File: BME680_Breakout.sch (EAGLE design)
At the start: 19 parts, among them U1 BME680, U4 PCA9515ADP, U8 LD1117XX

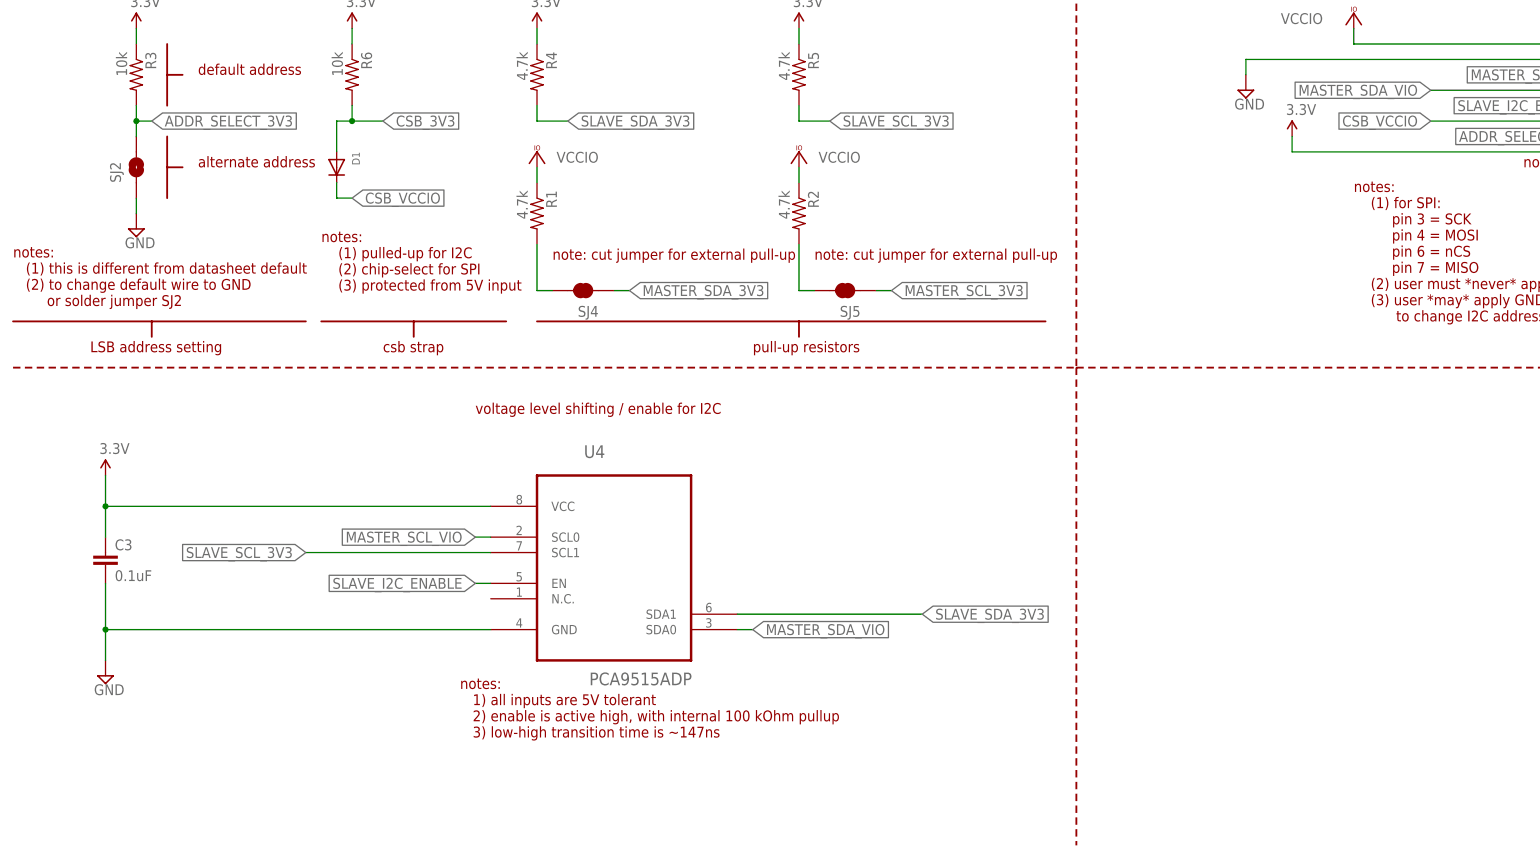
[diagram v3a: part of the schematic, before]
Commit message: added pull-down hardware option to allow changing default behavior of i2c buffer
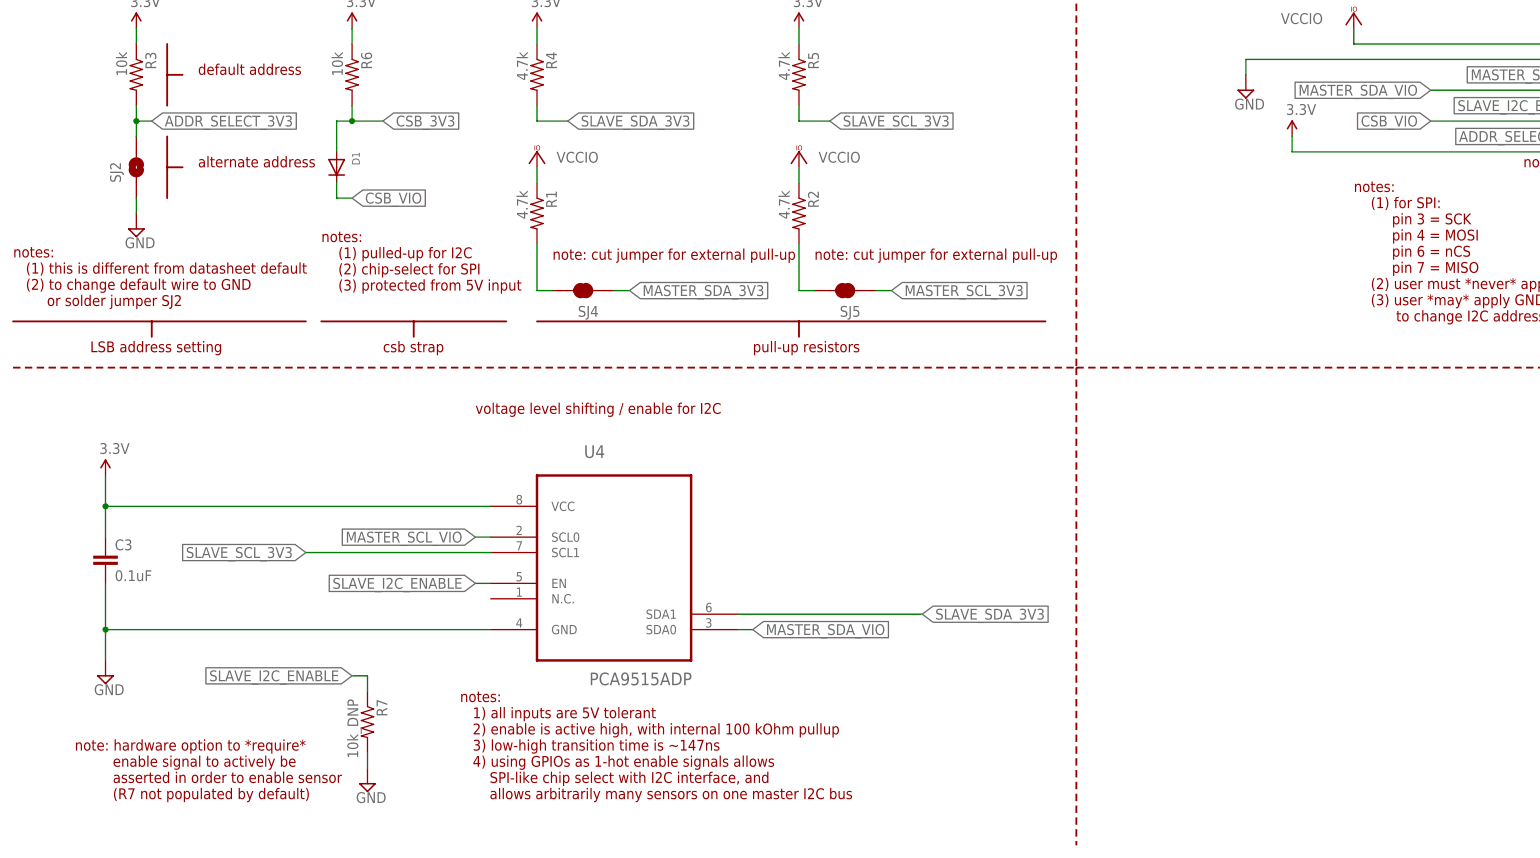
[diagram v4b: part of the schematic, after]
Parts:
- added R7: 10k_DNP, SparkFun-Passives:RESISTOR0805-RES
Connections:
- net CSB_VCCIO renamed CSB_VIO
- net GND: now also R7.2
- net SLAVE_I2C_ENABLE: now also R7.1
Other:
- note added: "note: hardware option to *require* enable signal to actively be asserted in order to enable sensor (R7 not populated by default)"
- note added: "notes: 1) all inputs are 5V tolerant 2) enable is active high, with internal 100 kOhm pullup 3) low-high transition time is ~147ns 4) using GPIOs as 1-hot enable signals allows SPI-like chip select with I2C interface, and allows arbitrarily many sensors on one master I2C bus"
- note removed: "notes: 1) all inputs are 5V tolerant 2) enable is active high, with internal 100 kOhm pullup 3) low-high transition time is ~147ns"
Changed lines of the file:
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@@
 <part name="C4" library="SparkFun-Passives" deviceset="CAP" device="0805" value="10uF"/>
 <part name="C5" library="SparkFun-Passives" deviceset="CAP" device="0805" value="10uF"/>
+<part name="R7" library="SparkFun-Passives" deviceset="RESISTOR" device="0805-RES" value="10k_DNP"/>
+<part name="SUPPLY16" library="supply2" deviceset="GND" device=""/>
 </parts>
 <sheets>
@@
     (2) chip-select for SPI
     (3) protected from 5V input</text>
-<text x="116.84" y="53.34" size="1.778" layer="94">notes:
+<text x="116.84" y="43.18" size="1.778" layer="94">notes:
    1) all inputs are 5V tolerant
    2) enable is active high, with internal 100 kOhm pullup
-   3) low-high transition time is ~147ns</text>
+   3) low-high transition time is ~147ns
+   4) using GPIOs as 1-hot enable signals allows
+       SPI-like chip select with I2C interface, and
+       allows arbitrarily many sensors on one master I2C bus</text>
 <text x="292.1" y="147.32" size="1.778" layer="94">note: output!</text>
 <text x="264.16" y="121.92" size="1.778" layer="94">notes:
@@
 <text x="132.08" y="132.08" size="1.778" layer="94">note: cut jumper for external pull-up</text>
 <text x="175.26" y="132.08" size="1.778" layer="94">note: cut jumper for external pull-up</text>
+<text x="53.34" y="43.18" size="1.778" layer="94">note: hardware option to *require*
+         enable signal to actively be
+         asserted in order to enable sensor
+         (R7 not populated by default)</text>
 </plain>
 <instances>
@@
 <instance part="C4" gate="G$1" x="264.16" y="215.9"/>
 <instance part="C5" gate="G$1" x="297.18" y="215.9"/>
+<instance part="R7" gate="G$1" x="101.6" y="55.88" rot="R270"/>
+<instance part="SUPPLY16" gate="GND" x="101.6" y="45.72"/>
 </instances>
 <busses>
@@
 <wire x1="297.18" y1="213.36" x2="297.18" y2="208.28" width="0.1524" layer="91"/>
 </segment>
+<segment>
+<pinref part="R7" gate="G$1" pin="2"/>
+<pinref part="SUPPLY16" gate="GND" pin="GND"/>
+<wire x1="101.6" y1="48.26" x2="101.6" y2="50.8" width="0.1524" layer="91"/>
+</segment>
 </net>
 <net name="CSB_3V3" class="0">
@@
 <wire x1="312.42" y1="157.48" x2="304.8" y2="157.48" width="0.1524" layer="91"/>
 </segment>
+<segment>
+<pinref part="R7" gate="G$1" pin="1"/>
+<wire x1="101.6" y1="60.96" x2="101.6" y2="63.5" width="0.1524" layer="91"/>
+<wire x1="101.6" y1="63.5" x2="99.06" y2="63.5" width="0.1524" layer="91"/>
+<label x="99.06" y="63.5" size="1.778" layer="95" rot="R180" xref="yes"/>
+</segment>
 </net>
 <net name="SLAVE_SDA_3V3" class="0">
@@
 </segment>
 </net>
-<net name="CSB_VCCIO" class="0">
+<net name="CSB_VIO" class="0">
 <segment>
 <pinref part="D1" gate="G$1" pin="C"/>

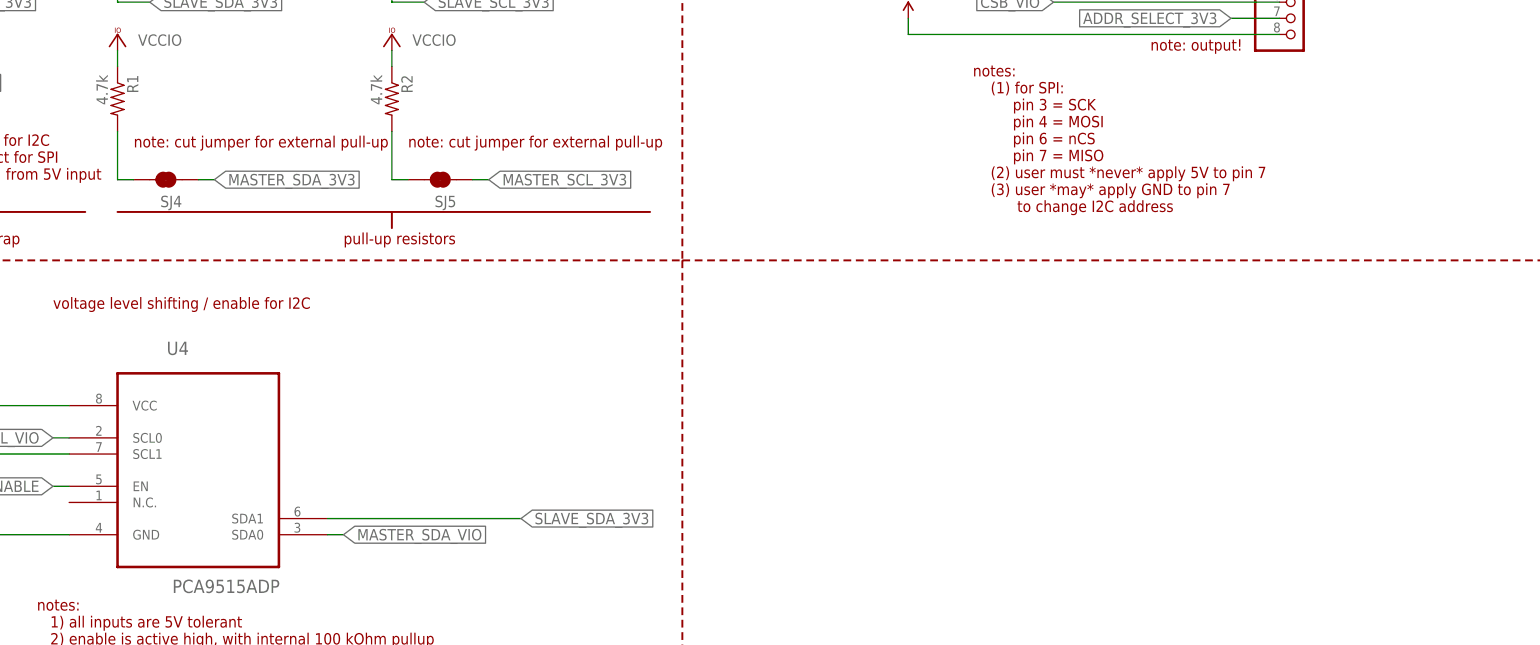
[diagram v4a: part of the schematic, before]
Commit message: added a few internal test points
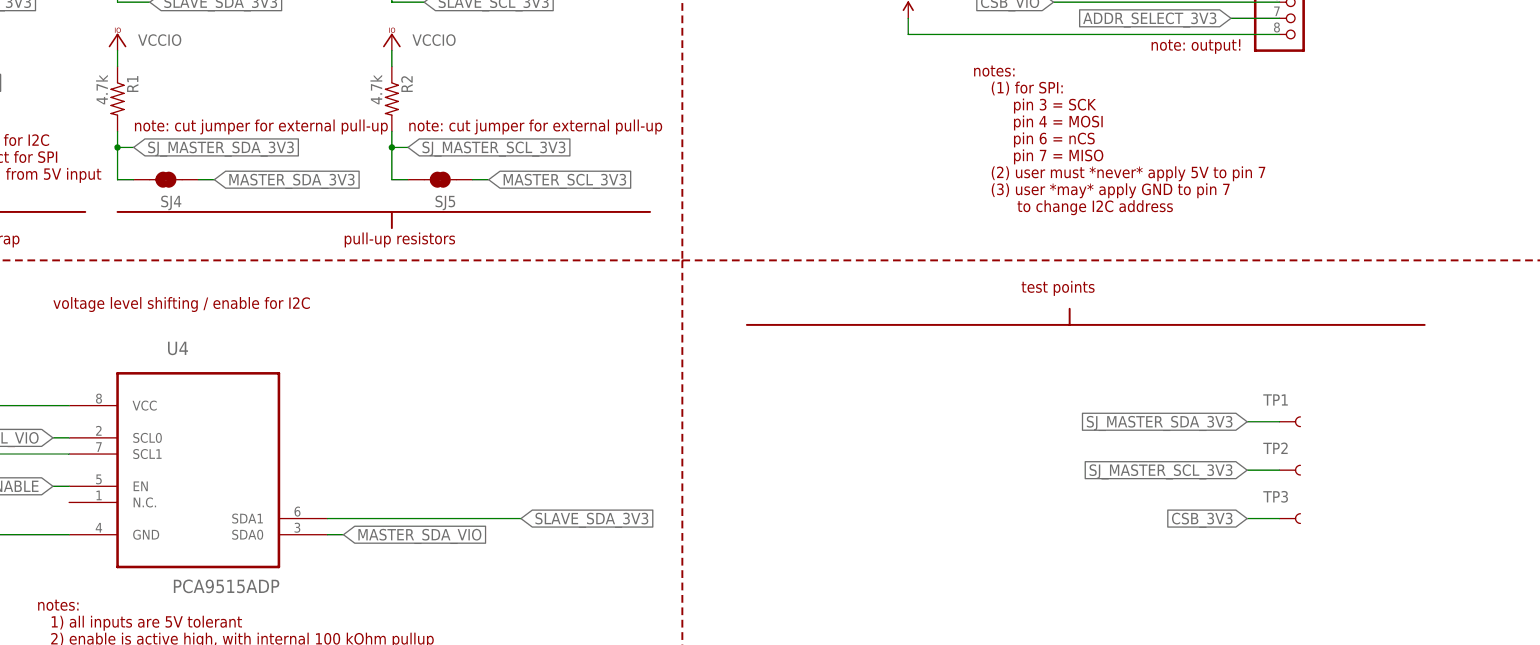
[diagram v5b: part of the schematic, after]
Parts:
- added TP1, TP2, TP3: TEST-POINT3X4, SparkFun-Passives:TEST-POINT3X4
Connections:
- removed net N$1: R1.2, SJ4.2
- removed net N$2: R2.2, SJ5.2
- new net SJ_MASTER_SCL_3V3: R2.2, SJ5.2, TP2.1
- new net SJ_MASTER_SDA_3V3: R1.2, SJ4.2, TP1.1
- net CSB_3V3: now also TP3.1
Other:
- note added: "test points"
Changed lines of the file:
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@@
 <part name="R7" library="SparkFun-Passives" deviceset="RESISTOR" device="0805-RES" value="10k_DNP"/>
 <part name="SUPPLY16" library="supply2" deviceset="GND" device=""/>
+<part name="TP1" library="SparkFun-Passives" deviceset="TEST-POINT" device="3X4"/>
+<part name="TP2" library="SparkFun-Passives" deviceset="TEST-POINT" device="3X4"/>
+<part name="TP3" library="SparkFun-Passives" deviceset="TEST-POINT" device="3X4"/>
 </parts>
 <sheets>
@@
 <wire x1="218.44" y1="187.96" x2="391.16" y2="187.96" width="0.3048" layer="94" style="longdash"/>
 <wire x1="43.18" y1="187.96" x2="218.44" y2="187.96" width="0.3048" layer="94" style="longdash"/>
-<text x="132.08" y="132.08" size="1.778" layer="94">note: cut jumper for external pull-up</text>
-<text x="175.26" y="132.08" size="1.778" layer="94">note: cut jumper for external pull-up</text>
+<text x="132.08" y="134.62" size="1.778" layer="94">note: cut jumper for external pull-up</text>
+<text x="175.26" y="134.62" size="1.778" layer="94">note: cut jumper for external pull-up</text>
 <text x="53.34" y="43.18" size="1.778" layer="94">note: hardware option to *require*
          enable signal to actively be
          asserted in order to enable sensor
          (R7 not populated by default)</text>
+<text x="271.78" y="109.22" size="1.778" layer="94">test points</text>
+<wire x1="228.6" y1="104.14" x2="279.4" y2="104.14" width="0.3048" layer="94"/>
+<wire x1="279.4" y1="104.14" x2="335.28" y2="104.14" width="0.3048" layer="94"/>
+<wire x1="279.4" y1="104.14" x2="279.4" y2="106.68" width="0.3048" layer="94"/>
 </plain>
 <instances>
@@
 <instance part="R7" gate="G$1" x="101.6" y="55.88" rot="R270"/>
 <instance part="SUPPLY16" gate="GND" x="101.6" y="45.72"/>
+<instance part="TP1" gate="G$1" x="312.42" y="88.9" smashed="yes">
+<attribute name="NAME" x="309.88" y="91.44" size="1.778" layer="95"/>
+</instance>
+<instance part="TP2" gate="G$1" x="312.42" y="81.28" smashed="yes">
+<attribute name="NAME" x="309.88" y="83.82" size="1.778" layer="95"/>
+</instance>
+<instance part="TP3" gate="G$1" x="312.42" y="73.66" smashed="yes">
+<attribute name="NAME" x="309.88" y="76.2" size="1.778" layer="95"/>
+</instance>
 </instances>
 <busses>
@@
 <wire x1="96.52" y1="154.94" x2="96.52" y2="149.86" width="0.1524" layer="91"/>
 </segment>
+<segment>
+<pinref part="TP3" gate="G$1" pin="1"/>
+<wire x1="312.42" y1="73.66" x2="307.34" y2="73.66" width="0.1524" layer="91"/>
+<label x="307.34" y="73.66" size="1.778" layer="95" rot="R180" xref="yes"/>
+</segment>
 </net>
 <net name="ADDR_SELECT_3V3" class="0">
@@
 </segment>
 </net>
-<net name="N$1" class="0">
+<net name="SJ_MASTER_SDA_3V3" class="0">
 <segment>
 <pinref part="R1" gate="G$1" pin="2"/>
 <pinref part="SJ4" gate="G$1" pin="2"/>
-<wire x1="129.54" y1="134.62" x2="129.54" y2="127" width="0.1524" layer="91"/>
+<wire x1="129.54" y1="134.62" x2="129.54" y2="132.08" width="0.1524" layer="91"/>
+<wire x1="129.54" y1="132.08" x2="129.54" y2="127" width="0.1524" layer="91"/>
 <wire x1="129.54" y1="127" x2="132.08" y2="127" width="0.1524" layer="91"/>
-</segment>
-</net>
-<net name="N$2" class="0">
+<wire x1="129.54" y1="132.08" x2="132.08" y2="132.08" width="0.1524" layer="91"/>
+<junction x="129.54" y="132.08"/>
+<label x="132.08" y="132.08" size="1.778" layer="95" xref="yes"/>
+</segment>
+<segment>
+<pinref part="TP1" gate="G$1" pin="1"/>
+<wire x1="312.42" y1="88.9" x2="307.34" y2="88.9" width="0.1524" layer="91"/>
+<label x="307.34" y="88.9" size="1.778" layer="95" rot="R180" xref="yes"/>
+</segment>
+</net>
+<net name="SJ_MASTER_SCL_3V3" class="0">
 <segment>
 <pinref part="R2" gate="G$1" pin="2"/>
 <pinref part="SJ5" gate="G$1" pin="2"/>
-<wire x1="172.72" y1="134.62" x2="172.72" y2="127" width="0.1524" layer="91"/>
+<wire x1="172.72" y1="134.62" x2="172.72" y2="132.08" width="0.1524" layer="91"/>
+<wire x1="172.72" y1="132.08" x2="172.72" y2="127" width="0.1524" layer="91"/>
 <wire x1="172.72" y1="127" x2="175.26" y2="127" width="0.1524" layer="91"/>
-</segment>
-</net>
+<wire x1="172.72" y1="132.08" x2="175.26" y2="132.08" width="0.1524" layer="91"/>
+<junction x="172.72" y="132.08"/>
+<label x="175.26" y="132.08" size="1.778" layer="95" xref="yes"/>
+</segment>
+<segment>
+<pinref part="TP2" gate="G$1" pin="1"/>
+<wire x1="312.42" y1="81.28" x2="307.34" y2="81.28" width="0.1524" layer="91"/>
+<label x="307.34" y="81.28" size="1.778" layer="95" rot="R180" xref="yes"/>
+</segment>
+</net>
